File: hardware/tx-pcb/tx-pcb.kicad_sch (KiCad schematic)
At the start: 63 parts, among them J1 Conn_To_J1, J2 Conn_To_J2, J3 BLIO, J4 Conn_01x05, J5 Conn_01x04, J6 PWRO, SW1 BOOT0, SW2 RESET, SW3 BTN1, SW4 BTN2, SW5 BTN3, SW6 BTN4, SW7 BTN5, U1 USBLC6-2SC6, U2 STM32WB55CEUx, X1 CS11336-32M, X2 ABS07-32.768KHZ-1-T

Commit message: finished tx layout v1.0
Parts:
- added J7: Conn_01x02_Pin, Connector_PinHeader_2.54mm:PinHeader_1x02_P2.54mm_Vertical, symbol Connector:Conn_01x02_Pin
- added SW8: SW_SPDT, rf-pwr-tx-library:spdt_amazon, symbol Switch:SW_SPDT
- added U3: (no value), rf-pwr-tx-library:TPS63070_board, symbol rf-pwr-tx-library:TPS63070_board
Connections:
- net +3V3: now also U3.3 (conv_out)
- net GND: now also J7.2 (Pin_2), U3.2 (gnd)
- net VBUS: now reaches R1.1, U1.5 (VBUS), USB1.A4B9 (VBUS), USB1.B4A9 (VBUS)
- net VBUS: now also SW8.3 (C)
- new net: J7.1 (Pin_1), SW8.1 (A)
- new net reg_in: SW8.2 (B), U3.1 (conv_in)
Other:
- note added: "5v from USB 6.4 - 2.4 from 4 cell alkaline [J7]"

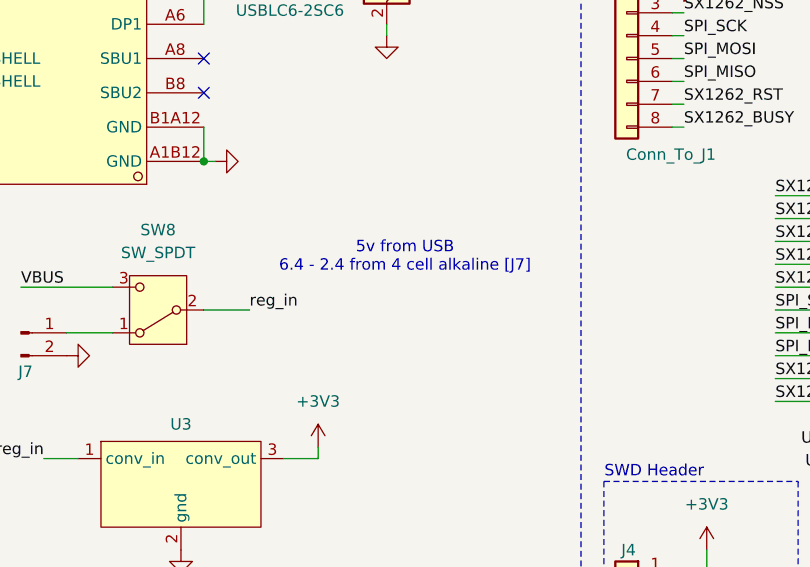
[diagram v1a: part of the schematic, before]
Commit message: updated power switch for tx board
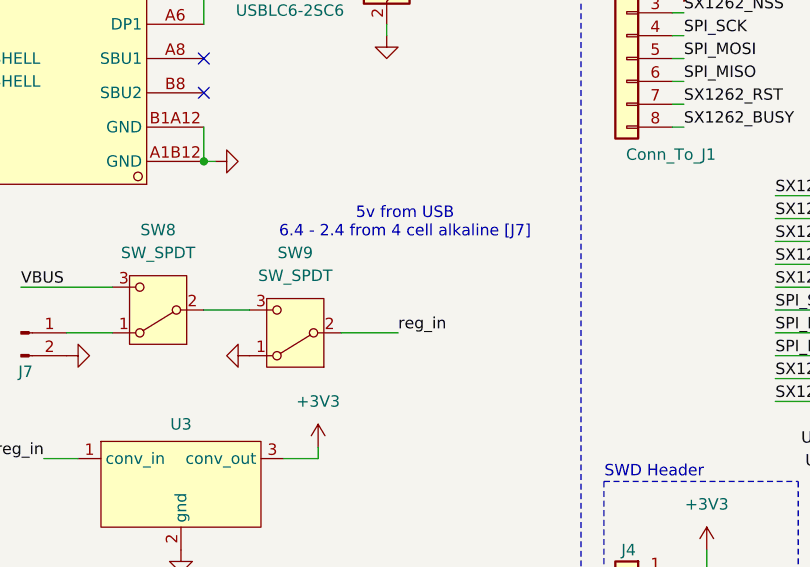
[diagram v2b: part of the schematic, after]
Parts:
- added SW9: SW_SPDT, rf-pwr-tx-library:spdt_amazon, symbol Switch:SW_SPDT
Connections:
- net GND: now also SW9.1 (A)
- net reg_in: now also SW9.2 (B); no longer SW8.2 (B)
- new net: SW8.2 (B), SW9.3 (C)
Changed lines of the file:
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@@
 	(text "5v from USB\n6.4 - 2.4 from 4 cell alkaline [J7]"
 		(exclude_from_sim no)
-		(at 65.532 79.248 0)
+		(at 65.532 75.438 0)
 		(effects
 			(font
@@
 	(wire
 		(pts
+			(xy 58.42 87.63) (xy 64.77 87.63)
+		)
+		(stroke
+			(width 0)
+			(type default)
+		)
+	)
+	(wire
+		(pts
 			(xy 214.63 140.97) (xy 218.44 140.97)
 		)
@@
 		)
 	)
+	(label "reg_in"
+		(at 64.77 87.63 0)
+		(effects
+			(font
+				(size 1.27 1.27)
+			)
+			(justify left bottom)
+		)
+	)
 	(label "USB_DM"
 		(at 116.84 100.33 180)
@@
 		)
 	)
-	(label "reg_in"
-		(at 48.26 85.09 0)
-		(effects
-			(font
-				(size 1.27 1.27)
-			)
-			(justify left bottom)
-		)
-	)
 	(label "SX1262_RFSW#"
 		(at 120.65 52.07 0)
@@
 	)
 	(symbol
+		(lib_id "Switch:SW_SPDT")
+		(at 53.34 87.63 180)
+		(unit 1)
+		(body_style 1)
+		(exclude_from_sim no)
+		(in_bom yes)
+		(on_board yes)
+		(in_pos_files yes)
+		(dnp no)
+		(fields_autoplaced yes)
+		(property "Reference" "SW9"
+			(at 53.34 78.74 0)
+			(show_name no)
+			(do_not_autoplace no)
+			(effects
+				(font
+					(size 1.27 1.27)
+				)
+			)
+		)
+		(property "Value" "SW_SPDT"
+			(at 53.34 81.28 0)
+			(show_name no)
+			(do_not_autoplace no)
+			(effects
+				(font
+					(size 1.27 1.27)
+				)
+			)
+		)
+		(property "Footprint" "rf-pwr-tx-library:spdt_amazon"
+			(at 53.34 87.63 0)
+			(hide yes)
+			(show_name no)
+			(do_not_autoplace no)
+			(effects
+				(font
+					(size 1.27 1.27)
+				)
+			)
+		)
+		(property "Datasheet" ""
+			(at 53.34 80.01 0)
+			(hide yes)
+			(show_name no)
+			(do_not_autoplace no)
+			(effects
+				(font
+					(size 1.27 1.27)
+				)
+			)
+		)
+		(property "Description" "Switch, single pole double throw"
+			(at 53.34 87.63 0)
+			(hide yes)
+			(show_name no)
+			(do_not_autoplace no)
+			(effects
+				(font
+					(size 1.27 1.27)
+				)
+			)
+		)
+		(pin "2"
+		)
+		(pin "1"
+		)
+		(pin "3"
+		)
+		(instances
+			(project "tx-pcb"
+				(path "/aa7f20e8-e05d-4c2a-a791-3275e92b22ea"
+					(reference "SW9")
+					(unit 1)
+				)
+			)
+		)
+	)
+	(symbol
 		(lib_id "power:GND")
 		(at 187.96 132.08 0)
@@
 					(unit 1)
 				)
+			)
+		)
+	)
+	(symbol
+		(lib_id "power:GND")
+		(at 48.26 90.17 270)
+		(unit 1)
+		(body_style 1)
+		(exclude_from_sim no)
+		(in_bom yes)
+		(on_board yes)
+		(in_pos_files yes)
+		(dnp no)
+		(fields_autoplaced yes)
+		(property "Reference" "#PWR052"
+			(at 41.91 90.17 0)
+			(hide yes)
+			(show_name no)
+			(do_not_autoplace no)
+			(effects
+				(font
+					(size 1.27 1.27)
+				)
+			)
+		)
+		(property "Value" "GND"
+			(at 43.18 90.17 0)
+			(hide yes)
+			(show_name no)
+			(do_not_autoplace no)
+			(effects
+				(font
+					(size 1.27 1.27)
+				)
+			)
+		)
+		(property "Footprint" ""
+			(at 48.26 90.17 0)
+			(hide yes)
+			(show_name no)
+			(do_not_autoplace no)
+			(effects
+				(font
+					(size 1.27 1.27)
+				)
+			)
+		)
+		(property "Datasheet" ""
+			(at 48.26 90.17 0)
+			(hide yes)
+			(show_name no)
+			(do_not_autoplace no)
+			(effects
+				(font
+					(size 1.27 1.27)
+				)
+			)
+		)
+		(property "Description" "Power symbol creates a global label with name \"GND\" , ground"
+			(at 48.26 90.17 0)
+			(hide yes)
+			(show_name no)
+			(do_not_autoplace no)
+			(effects
+				(font
+					(size 1.27 1.27)
+				)
+			)
+		)
+		(pin "1"
+		)
+		(instances
+			(project "tx-pcb"
+				(path "/aa7f20e8-e05d-4c2a-a791-3275e92b22ea"
+					(reference "#PWR052")
+					(unit 1)
+				)

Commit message: double checked for purchase
updated TX SPI_CLK pin, was incorrect
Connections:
- net SPI_SCK: now also U2.10 (PA1); no longer U2.14 (PA5)
- net SX1262_BUSY: now also U2.11 (PA2); no longer U2.10 (PA1)
- net SX1262_DIO2: now also U2.12 (PA3); no longer U2.11 (PA2)
- net SX1262_RFSW: now also U2.14 (PA5); no longer U2.13 (PA4)
- net SX1262_RST: now also U2.13 (PA4); no longer U2.12 (PA3)
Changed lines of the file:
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@@
+	(wire
+		(pts
+			(xy 106.68 74.93) (xy 124.46 74.93)
+		)
+		(stroke
+			(width 0)
+			(type default)
+		)
+	)
 	(wire
 		(pts
@@
 		(pts
 			(xy 146.05 189.23) (xy 146.05 190.5)
-		)
-		(stroke
-			(width 0)
-			(type default)
-		)
-	)
-	(wire
-		(pts
-			(xy 106.68 74.93) (xy 124.46 74.93)
 		)
 		(stroke
@@
 		)
 	)
-	(label "SX1262_RFSW"
-		(at 106.68 82.55 0)
-		(effects
-			(font
-				(size 1.27 1.27)
-			)
-			(justify left bottom)
-		)
-	)
 	(label "SWD_NSRT"
 		(at 38.1 143.51 0)
@@
 		)
 	)
-	(label "SX1262_DIO2"
-		(at 106.68 77.47 0)
-		(effects
-			(font
-				(size 1.27 1.27)
-			)
-			(justify left bottom)
-		)
-	)
 	(label "SMPSFB"
 		(at 170.18 90.17 0)
@@
 	)
 	(label "SX1262_BUSY"
+		(at 106.68 77.47 0)
+		(effects
+			(font
+				(size 1.27 1.27)
+			)
+			(justify left bottom)
+		)
+	)
+	(label "SX1262_BUSY"
 		(at 96.52 64.77 0)
 		(effects
@@
 		)
 	)
+	(label "SX1262_RFSW"
+		(at 106.68 85.09 0)
+		(effects
+			(font
+				(size 1.27 1.27)
+			)
+			(justify left bottom)
+		)
+	)
+	(label "SPI_SCK"
+		(at 106.68 74.93 0)
+		(effects
+			(font
+				(size 1.27 1.27)
+			)
+			(justify left bottom)
+		)
+	)
 	(label "VBUS"
 		(at 22.86 82.55 0)
@@
 		)
 	)
+	(label "SX1262_DIO2"
+		(at 106.68 80.01 0)
+		(effects
+			(font
+				(size 1.27 1.27)
+			)
+			(justify left bottom)
+		)
+	)
 	(label "I2C1_SDA"
 		(at 105.41 158.75 180)
@@
 		)
 	)
-	(label "SPI_SCK"
-		(at 106.68 85.09 0)
-		(effects
-			(font
-				(size 1.27 1.27)
-			)
-			(justify left bottom)
-		)
-	)
 	(label "SPI_MOSI"
 		(at 96.52 57.15 0)
@@
 		)
 	)
-	(label "SX1262_RST"
-		(at 106.68 80.01 0)
-		(effects
-			(font
-				(size 1.27 1.27)
-			)
-			(justify left bottom)
-		)
-	)
 	(label "SWCLK"
 		(at 99.06 116.84 0)
@@
 		)
 	)
+	(label "SX1262_RST"
+		(at 106.68 82.55 0)
+		(effects
+			(font
+				(size 1.27 1.27)
+			)
+			(justify left bottom)
+		)
+	)
 	(label "BTN4"
 		(at 125.73 180.34 0)
 		(effects
 			(font
-				(size 1.27 1.27)
-			)
-			(justify left bottom)
-		)
-	)
-	(label "SX1262_BUSY"
-		(at 106.68 74.93 0)
-		(effects
-			(font

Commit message: updates for dr weeks
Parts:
- removed D1: LED, LED_SMD:LED_0603_1608Metric_Pad1.05x0.95mm_HandSolder, symbol Device:LED
- removed R1: 10k, Resistor_SMD:R_0805_2012Metric_Pad1.20x1.40mm_HandSolder, symbol Device:R
- removed R2: 5k1, Resistor_SMD:R_0805_2012Metric_Pad1.20x1.40mm_HandSolder, symbol Device:R
- removed SW8: SW_SPDT, rf-pwr-tx-library:spdt_amazon, symbol Switch:SW_SPDT
- removed U1: USBLC6-2SC6, Package_TO_SOT_SMD:SOT-23-6, symbol Power_Protection:USBLC6-2SC6
- removed USB1: GT-USB-7047A, rf-pwr-tx-library:USB-C-SMD_GT-USB-7047A, symbol rf-pwr-tx-library:GT-USB-7047A
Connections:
- net at J7.1 (Pin_1): now also SW9.3 (C)
- no-connect marks 8 -> 6
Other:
- note added: "SDR Config"
- note removed: "5k1 R's tell the computer there is a power-sinking device connected"
- note removed: "ESD Protection"
- note removed: "USB PWR GOOD"
- moved on the sheet: C25, C26, J1, J2, J4, J6, J7, L5, SW9, U3

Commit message: fixed HSE induction loop
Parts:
- removed X1: CS11336-32M, rf-pwr-tx-library:NX2016SA_NDK, symbol rx-parts:Q22FA12800025
- added X1: Q22FA12800025, easyeda2kicad:CRYSTAL-SMD_4P-L2.0-W1.6-BL, symbol easyeda2kicad:Q22FA12800025
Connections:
- net GND: now also X1.2 (GND), X1.4 (GND)
- net HSE_OSC_IN: now also X1.1
- net HSE_OSC_OUT: now also X1.3
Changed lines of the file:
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@@
 	)
 	(symbol
-		(lib_id "rx-parts:Q22FA12800025")
-		(at 193.04 80.01 0)
-		(unit 1)
-		(body_style 1)
-		(exclude_from_sim no)
-		(in_bom yes)
-		(on_board yes)
-		(in_pos_files yes)
-		(dnp no)
-		(property "Reference" "X1"
-			(at 196.85 73.914 0)
-			(show_name no)
-			(do_not_autoplace no)
-			(effects
-				(font
-					(size 1.27 1.27)
-				)
-			)
-		)
-		(property "Value" "CS11336-32M"
-			(at 193.294 86.868 0)
-			(show_name no)
-			(do_not_autoplace no)
-			(effects
-				(font
-					(size 1.27 1.27)
-				)
-			)
-		)
-		(property "Footprint" "rf-pwr-tx-library:NX2016SA_NDK"
-			(at 193.04 90.17 0)
-			(hide yes)
-			(show_name no)
-			(do_not_autoplace no)
-			(effects
-				(font
-					(size 1.27 1.27)
-				)
-			)
-		)
-		(property "Datasheet" "https://lcsc.com/product-detail/SMD-Crystals_EPSON_Q22FA12800025_FA-128-32MHZ-8PF-10ppm_C187794.html"
-			(at 193.04 92.71 0)
-			(hide yes)
-			(show_name no)
-			(do_not_autoplace no)
-			(effects
-				(font
-					(size 1.27 1.27)
-				)
-			)
-		)
-		(property "Description" ""
-			(at 193.04 80.01 0)
-			(hide yes)
-			(show_name no)
-			(do_not_autoplace no)
-			(effects
-				(font
-					(size 1.27 1.27)
-				)
-			)
-		)
-		(property "Manufacturer" "EPSON(爱普生)"
-			(at 193.04 95.25 0)
-			(hide yes)
-			(show_name no)
-			(do_not_autoplace no)
-			(effects
-				(font
-					(size 1.27 1.27)
-				)
-			)
-		)
-		(property "MPN" "Q22FA12800025"
-			(at 193.04 97.79 0)
-			(hide yes)
-			(show_name no)
-			(do_not_autoplace no)
-			(effects
-				(font
-					(size 1.27 1.27)
-				)
-			)
-		)
-		(property "LCSC Part" "C187794"
-			(at 193.04 100.33 0)
-			(hide yes)
-			(show_name no)
-			(do_not_autoplace no)
-			(effects
-				(font
-					(size 1.27 1.27)
-				)
-			)
-		)
-		(pin "3"
-		)
-		(pin "4"
-		)
-		(pin "2"
-		)
-		(pin "1"
-		)
-		(instances
-			(project "tx-pcb"
-				(path "/aa7f20e8-e05d-4c2a-a791-3275e92b22ea"
-					(reference "X1")
-					(unit 1)
-				)
-			)
-		)
-	)
-	(symbol
 		(lib_id "Connector_Generic:Conn_01x04")
 		(at 90.17 153.67 0)
@@
 					(unit 1)
 				)
+			)
+		)
+	)
+	(symbol
+		(lib_id "easyeda2kicad:Q22FA12800025")
+		(at 193.04 80.01 0)
+		(unit 1)
+		(body_style 1)
+		(exclude_from_sim no)
+		(in_bom yes)
+		(on_board yes)
+		(in_pos_files yes)
+		(dnp no)
+		(property "Reference" "X1"
+			(at 193.04 71.374 0)
+			(show_name no)
+			(do_not_autoplace no)
+			(effects
+				(font
+					(size 1.27 1.27)
+				)
+			)
+		)
+		(property "Value" "Q22FA12800025"
+			(at 193.04 73.914 0)
+			(show_name no)
+			(do_not_autoplace no)
+			(effects
+				(font
+					(size 1.27 1.27)
+				)
+			)
+		)
+		(property "Footprint" "easyeda2kicad:CRYSTAL-SMD_4P-L2.0-W1.6-BL"
+			(at 193.04 90.17 0)
+			(hide yes)
+			(show_name no)
+			(do_not_autoplace no)
+			(effects
+				(font
+					(size 1.27 1.27)
+				)
+			)
+		)
+		(property "Datasheet" "https://lcsc.com/product-detail/SMD-Crystals_EPSON_Q22FA12800025_FA-128-32MHZ-8PF-10ppm_C187794.html"
+			(at 193.04 92.71 0)
+			(hide yes)
+			(show_name no)
+			(do_not_autoplace no)
+			(effects
+				(font
+					(size 1.27 1.27)
+				)
+			)
+		)
+		(property "Description" ""
+			(at 193.04 80.01 0)
+			(hide yes)
+			(show_name no)
+			(do_not_autoplace no)
+			(effects
+				(font
+					(size 1.27 1.27)
+				)
+			)
+		)
+		(property "Manufacturer" "EPSON(爱普生)"
+			(at 193.04 95.25 0)
+			(hide yes)
+			(show_name no)
+			(do_not_autoplace no)
+			(effects
+				(font
+					(size 1.27 1.27)
+				)
+			)
+		)
+		(property "MPN" "Q22FA12800025"
+			(at 193.04 97.79 0)
+			(hide yes)
+			(show_name no)
+			(do_not_autoplace no)
+			(effects
+				(font
+					(size 1.27 1.27)
+				)
+			)
+		)
+		(property "LCSC Part" "C187794"
+			(at 193.04 100.33 0)
+			(hide yes)
+			(show_name no)
+			(do_not_autoplace no)
+			(effects
+				(font
+					(size 1.27 1.27)
+				)
+			)
+		)
+		(pin "3"
+		)
+		(pin "4"
+		)
+		(pin "2"
+		)
+		(pin "1"
+		)
+		(instances
+			(project "tx-pcb"
+				(path "/aa7f20e8-e05d-4c2a-a791-3275e92b22ea"
+					(reference "X1")
+					(unit 1)
+				)

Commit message: updated bluetooth output for MLPF chip and fixed ground layer issue
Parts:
- removed C12: 0.8p, Capacitor_SMD:C_0603_1608Metric_Pad1.08x0.95mm_HandSolder, symbol Device:C
- removed C13: 0.3p, Capacitor_SMD:C_0603_1608Metric_Pad1.08x0.95mm_HandSolder, symbol Device:C
- removed C14, C15: NC, Capacitor_SMD:C_0603_1608Metric_Pad1.08x0.95mm_HandSolder, symbol Device:C
- removed C25, C26: C, Capacitor_SMD:C_0603_1608Metric_Pad1.08x0.95mm_HandSolder, symbol Device:C
- removed FL1: DLF162500LT-5028A1, rf-pwr-tx-library:FILTER-SMD_6P-L1.6-W1.0-P0.50-BL, symbol easyeda2kicad:DLF162500LT-5028A1
- removed J1: Conn_To_J1, Connector_PinHeader_2.54mm:PinHeader_1x08_P2.54mm_Vertical, symbol Connector_Generic:Conn_01x08
- removed J6: PWRO, Connector_Coaxial:SMA_BAT_Wireless_BWSMA-KWE-Z001, symbol Connector:Conn_Coaxial_Small
- removed L3: 2.7n, Inductor_SMD:L_0805_2012Metric_Pad1.05x1.20mm_HandSolder, symbol Device:L
- removed L4: 0R, Inductor_SMD:L_0805_2012Metric_Pad1.05x1.20mm_HandSolder, symbol Device:L
- removed L5: L, Inductor_SMD:L_0805_2012Metric_Pad1.05x1.20mm_HandSolder, symbol Device:L
- added FL1: MLPF-WB-01D3, easyeda2kicad:BGA-6_L1.6-W1.0-R3-C2-P0.50-TL, symbol easyeda2kicad:MLPF-WB-01D3
- added J1: Conn_01x07, Connector_PinHeader_2.54mm:PinHeader_1x07_P2.54mm_Vertical, symbol Connector_Generic:Conn_01x07
- J3: footprint Connector_Coaxial:SMA_BAT_Wireless_BWSMA-KWE-Z001 -> SMA_Samtec_SMA-J-P-H-ST-EM1_EdgeMount
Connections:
- net GND: now also J4.2 (Pin_2), FL1.A2 (GND4), FL1.B1 (GND3), FL1.B2 (GND2), FL1.B3 (GND1), J1.7 (Pin_7); no longer J4.3 (Pin_3)
- net RF1_IN: now also FL1.A3 (IN)
- net SPI_MISO: now also J1.3 (Pin_3)
- net SPI_MOSI: now also J1.4 (Pin_4)
- net SPI_SCK: now also J1.5 (Pin_5)
- net SWCLK: now also J4.3 (Pin_3); no longer J4.2 (Pin_2)
- net SX1262_BUSY: now also J1.1 (Pin_1)
- net SX1262_NSS: now also J1.6 (Pin_6)
- net SX1262_RST: now also J1.2 (Pin_2)
- net at J3.1 (In): now also FL1.A1 (OUT)
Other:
- moved on the sheet: J2
